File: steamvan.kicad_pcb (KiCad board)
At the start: 2 copper layers, 243.4 x 76.7 mm, 188 parts, among them J1 Conn_01x05_Male, Q1 FMMT493TA, SW1 SW_Push, U1 STM32F303CBTx, U2 TLV70233_SOT23-5, U3 NUF2221W1T2G, U4 74LVC1G34, Y1 8MHz

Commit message: Update: Move more components
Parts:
- moved R40 1.10 mm to (143.4, 127.0)
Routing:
- net Net-(K_SUPER1-Pad4): track 10.2 -> 8.71 mm
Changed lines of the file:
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@@
     (thickness 1.6)
     (drawings 6)
-    (tracks 2157)
+    (tracks 2158)
     (zones 0)
     (modules 188)
@@
   )
   (module Resistor_SMD:R_0603_1608Metric (layer B.Cu)
-    (at 144.4625 127 90)
+    (at 143.3576 127 90)
     (descr "Resistor SMD 0603 (1608 Metric), square (rectangular) end terminal, IPC_7351 nominal, (Body size source: http://www.tortai-tech.com/upload/download/2011102023233369053.pdf), generated with kicad-footprint-generator")
     (tags resistor)
@@
   (via (at 233.299 107.442) (size 0.8) (drill 0.4) (layers F.Cu B.Cu) (net 2))
   (via (at 218.313 127.381) (size 0.8) (drill 0.4) (layers F.Cu B.Cu) (net 2))
-  (via (at 142.367 128.27) (size 0.8) (drill 0.4) (layers F.Cu B.Cu) (net 2))
+  (via (at 141.3764 128.4224) (size 0.8) (drill 0.4) (layers F.Cu B.Cu) (net 2))
   (via (at 97.282 110.617) (size 0.8) (drill 0.4) (layers F.Cu B.Cu) (net 2))
   (via (at 203.0984 127) (size 0.8) (drill 0.4) (layers F.Cu B.Cu) (net 2))
@@
   (segment (start 211.29 127.7875) (end 210.82 127.3175) (width 0.381) (layer B.Cu) (net 83) (status 30))
   (segment (start 215.9 127.7875) (end 211.29 127.7875) (width 0.381) (layer B.Cu) (net 83) (status 30))
-  (segment (start 144.4625 127.7875) (end 144.4625 128.4605) (width 0.381) (layer B.Cu) (net 84) (status 10))
-  (segment (start 144.4625 128.4605) (end 143.637 129.286) (width 0.381) (layer B.Cu) (net 84))
-  (segment (start 136.8425 128.651) (end 136.8425 127.3175) (width 0.381) (layer B.Cu) (net 84) (status 20))
-  (segment (start 137.4775 129.286) (end 136.8425 128.651) (width 0.381) (layer B.Cu) (net 84))
-  (segment (start 143.637 129.286) (end 137.4775 129.286) (width 0.381) (layer B.Cu) (net 84))
+  (segment (start 143.3576 127.7875) (end 143.3576 128.27) (width 0.381) (layer B.Cu) (net 84))
+  (segment (start 143.3576 127.7875) (end 143.3576 128.1176) (width 0.381) (layer B.Cu) (net 84))
+  (segment (start 143.3576 128.1176) (end 142.0876 129.3876) (width 0.381) (layer B.Cu) (net 84))
+  (segment (start 138.9126 129.3876) (end 136.8425 127.3175) (width 0.381) (layer B.Cu) (net 84))
+  (segment (start 142.0876 129.3876) (end 138.9126 129.3876) (width 0.381) (layer B.Cu) (net 84))
   (segment (start 178.689 68.961) (end 177.4825 70.1675) (width 0.381) (layer B.Cu) (net 85) (status 20))
   (segment (start 184.15 70.6375) (end 182.4735 68.961) (width 0.381) (layer B.Cu) (net 85) (status 10))
@@
   (segment (start 160.3375 107.1625) (end 160.9345 107.1625) (width 0.381) (layer B.Cu) (net 93) (status 10))
   (segment (start 160.9345 107.1625) (end 161.798 106.299) (width 0.381) (layer B.Cu) (net 93))
-  (segment (start 174.58065 125.3744) (end 175.41875 126.2125) (width 0.381) (layer B.Cu) (net 93) (status 20))
-  (segment (start 144.4625 126.2125) (end 145.3006 125.3744) (width 0.381) (layer B.Cu) (net 93) (status 10))
-  (segment (start 145.3006 125.3744) (end 174.58065 125.3744) (width 0.381) (layer B.Cu) (net 93))
-  (segment (start 123.825 126.2125) (end 124.675789 125.361711) (width 0.381) (layer B.Cu) (net 93) (status 10))
-  (segment (start 143.611711 125.361711) (end 144.4625 126.2125) (width 0.381) (layer B.Cu) (net 93) (status 20))
-  (segment (start 124.675789 125.361711) (end 143.611711 125.361711) (width 0.381) (layer B.Cu) (net 93))
   (segment (start 283.7688 86.4362) (end 283.7688 78.0288) (width 0.381) (layer F.Cu) (net 93))
   (via (at 278.384 70.231) (size 0.8) (drill 0.4) (layers F.Cu B.Cu) (net 93))
@@
   (segment (start 274.828 124.7775) (end 273.361099 126.244401) (width 0.381) (layer F.Cu) (net 93))
   (segment (start 271.113785 107.3023) (end 275.113711 111.302226) (width 0.381) (layer F.Cu) (net 93))
+  (segment (start 144.1957 125.3744) (end 143.3576 126.2125) (width 0.381) (layer B.Cu) (net 93))
+  (segment (start 175.41875 126.2125) (end 174.58065 125.3744) (width 0.381) (layer B.Cu) (net 93))
+  (segment (start 174.58065 125.3744) (end 144.1957 125.3744) (width 0.381) (layer B.Cu) (net 93))
+  (segment (start 123.825 126.2125) (end 132.8167 126.2125) (width 0.381) (layer B.Cu) (net 93))
+  (segment (start 132.8167 126.2125) (end 133.4516 125.5776) (width 0.381) (layer B.Cu) (net 93))
+  (segment (start 142.7227 125.5776) (end 143.3576 126.2125) (width 0.381) (layer B.Cu) (net 93))
+  (segment (start 133.4516 125.5776) (end 142.7227 125.5776) (width 0.381) (layer B.Cu) (net 93))
   (segment (start 276.7836 77.3684) (end 275.844 78.308) (width 0.254) (layer B.Cu) (net 94) (status 20))
   (segment (start 282.8576 77.3684) (end 276.7836 77.3684) (width 0.254) (layer B.Cu) (net 94))

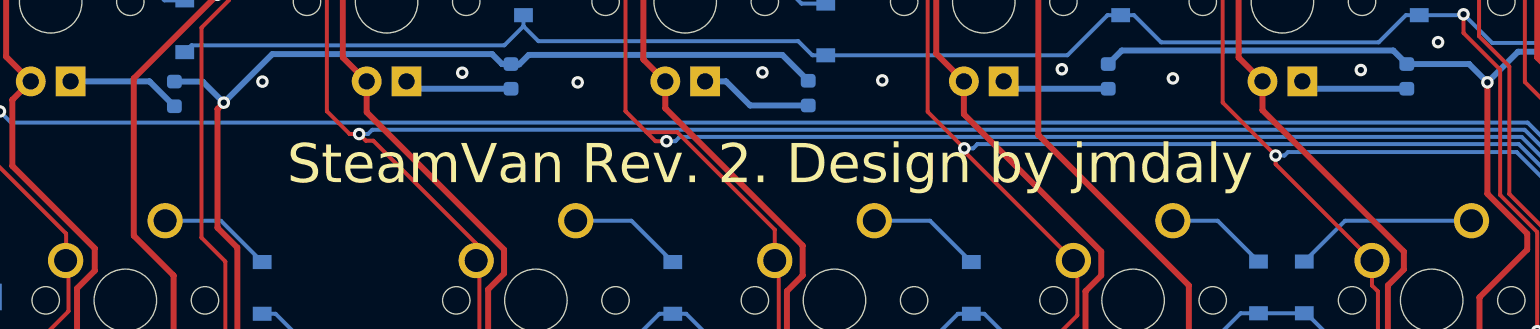
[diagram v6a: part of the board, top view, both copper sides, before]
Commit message: Update: Files for KiCad 5.1
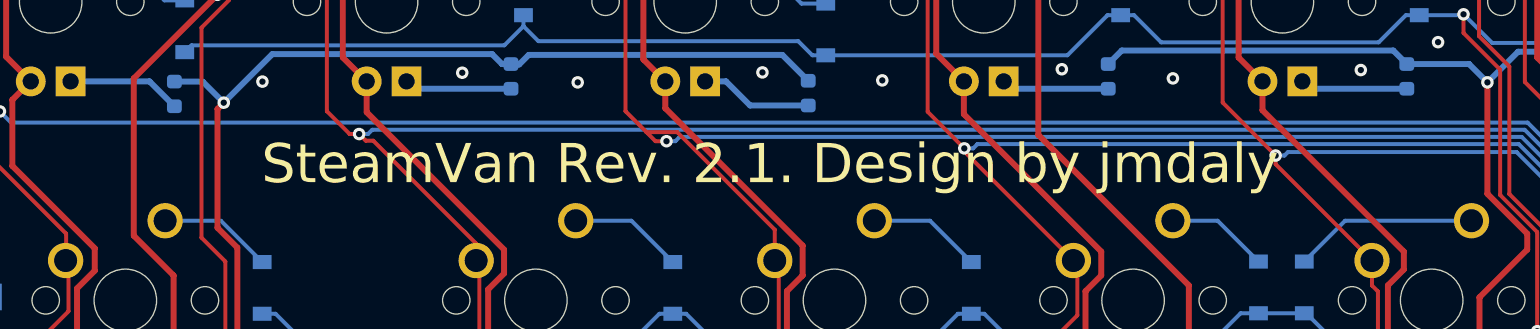
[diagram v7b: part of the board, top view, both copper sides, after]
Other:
- board text added: "SteamVan Rev. 2.1. Design by jmdaly"
- board text removed: "SteamVan Rev. 2. Design by jmdaly"
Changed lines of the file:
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@@
-(kicad_pcb (version 20171130) (host pcbnew 5.0.2-bee76a0~70~ubuntu16.04.1)
+(kicad_pcb (version 20171130) (host pcbnew 5.1.5-52549c5~84~ubuntu16.04.1)
   (general
     (thickness 1.6)
@@
     (zone_45_only no)
     (trace_min 0.2)
-    (segment_width 0.2)
-    (edge_width 0.15)
     (via_size 0.8)
     (via_drill 0.4)
@@
     (uvia_min_size 0.2)
     (uvia_min_drill 0.1)
+    (edge_width 0.15)
+    (segment_width 0.2)
     (pcb_text_width 0.3)
     (pcb_text_size 1.5 1.5)
@@
     (add_net "Net-(K_Z1-Pad4)")
   )
+  (module Type-C:HRO-TYPE-C-31-M-12-Assembly (layer B.Cu)
+    (at 284.584 53.646)
+    (attr smd)
+    (fp_text reference USB1 (at 0 9.25) (layer B.SilkS)
+      (effects (font (size 1 1) (thickness 0.15)) (justify mirror))
+    )
+    (fp_text value HRO-TYPE-C-31-M-12 (at 0 -1.15) (layer Dwgs.User)
+      (effects (font (size 1 1) (thickness 0.15)))
+    )
+    (fp_line (start 3.75 8.5) (end 3.75 7.5) (layer B.CrtYd) (width 0.15))
+    (fp_line (start -3.75 8.5) (end 3.75 8.5) (layer B.CrtYd) (width 0.15))
+    (fp_line (start -3.75 7.5) (end -3.75 8.5) (layer B.CrtYd) (width 0.15))
+    (fp_line (start -4.5 0) (end -4.5 7.5) (layer B.CrtYd) (width 0.15))
+    (fp_line (start 4.5 0) (end -4.5 0) (layer B.CrtYd) (width 0.15))
+    (fp_line (start 4.5 7.5) (end 4.5 0) (layer B.CrtYd) (width 0.15))
+    (fp_line (start 3.75 7.5) (end 4.5 7.5) (layer B.CrtYd) (width 0.15))
+    (fp_line (start -4.5 7.5) (end -3.75 7.5) (layer B.CrtYd) (width 0.15))
+    (fp_text user %R (at 0 9.25) (layer B.Fab)
+      (effects (font (size 1 1) (thickness 0.15)) (justify mirror))
+    )
+    (fp_line (start -4.47 0) (end 4.47 0) (layer Dwgs.User) (width 0.15))
+    (fp_line (start -4.47 0) (end -4.47 7.3) (layer Dwgs.User) (width 0.15))
+    (fp_line (start 4.47 0) (end 4.47 7.3) (layer Dwgs.User) (width 0.15))
+    (fp_line (start -4.47 7.3) (end 4.47 7.3) (layer Dwgs.User) (width 0.15))
+    (pad 12 smd rect (at 3.225 7.695) (size 0.6 1.45) (layers B.Cu B.Paste B.Mask)
+      (net 2 GND))
+    (pad 1 smd rect (at -3.225 7.695) (size 0.6 1.45) (layers B.Cu B.Paste B.Mask)
+      (net 2 GND))
+    (pad 11 smd rect (at 2.45 7.695) (size 0.6 1.45) (layers B.Cu B.Paste B.Mask)
+      (net 34 "Net-(F1-Pad2)"))
+    (pad 2 smd rect (at -2.45 7.695) (size 0.6 1.45) (layers B.Cu B.Paste B.Mask)
+      (net 34 "Net-(F1-Pad2)"))
+    (pad 3 smd rect (at -1.75 7.695) (size 0.3 1.45) (layers B.Cu B.Paste B.Mask)
+      (net 112 "Net-(USB1-Pad3)"))
+    (pad 10 smd rect (at 1.75 7.695) (size 0.3 1.45) (layers B.Cu B.Paste B.Mask)
+      (net 97 "Net-(RC7-Pad2)"))
+    (pad 4 smd rect (at -1.25 7.695) (size 0.3 1.45) (layers B.Cu B.Paste B.Mask)
+      (net 96 "Net-(RC6-Pad2)"))
+    (pad 9 smd rect (at 1.25 7.695) (size 0.3 1.45) (layers B.Cu B.Paste B.Mask)
+      (net 111 "Net-(USB1-Pad9)"))
+    (pad 5 smd rect (at -0.75 7.695) (size 0.3 1.45) (layers B.Cu B.Paste B.Mask)
+      (net 110 D_NI))
+    (pad 8 smd rect (at 0.75 7.695) (size 0.3 1.45) (layers B.Cu B.Paste B.Mask)
+      (net 109 D_PI))
+    (pad 7 smd rect (at 0.25 7.695) (size 0.3 1.45) (layers B.Cu B.Paste B.Mask)
+      (net 110 D_NI))
+    (pad 6 smd rect (at -0.25 7.695) (size 0.3 1.45) (layers B.Cu B.Paste B.Mask)
+      (net 109 D_PI))
+    (pad "" np_thru_hole circle (at 2.89 6.25) (size 0.65 0.65) (drill 0.65) (layers *.Cu *.Mask))
+    (pad "" np_thru_hole circle (at -2.89 6.25) (size 0.65 0.65) (drill 0.65) (layers *.Cu *.Mask))
+    (pad 13 thru_hole oval (at -4.32 6.78) (size 1 2.1) (drill oval 0.6 1.7) (layers *.Cu *.Mask)
+      (net 2 GND))
+    (pad 13 thru_hole oval (at 4.32 6.78) (size 1 2.1) (drill oval 0.6 1.7) (layers *.Cu *.Mask)
+      (net 2 GND))
+    (pad 13 thru_hole oval (at -4.32 2.6) (size 1 1.6) (drill oval 0.6 1.2) (layers *.Cu *.Mask)
+      (net 2 GND))
+    (pad 13 thru_hole oval (at 4.32 2.6) (size 1 1.6) (drill oval 0.6 1.2) (layers *.Cu *.Mask)
+      (net 2 GND))
+  )
   (module jmdaly_keyboard_parts:minivan_outline locked (layer F.Cu)
     (at 102.84 74.63)
@@
       (net 105 D_N))
   )
-  (module Type-C:HRO-TYPE-C-31-M-12-Assembly (layer B.Cu)
-    (at 284.584 53.646)
-    (fp_text reference USB1 (at 0 9.25) (layer B.SilkS)
-      (effects (font (size 1 1) (thickness 0.15)) (justify mirror))
-    )
-    (fp_text value HRO-TYPE-C-31-M-12 (at 0 -1.15) (layer Dwgs.User)
-      (effects (font (size 1 1) (thickness 0.15)))
-    )
-    (fp_line (start -4.47 7.3) (end 4.47 7.3) (layer Dwgs.User) (width 0.15))
-    (fp_line (start 4.47 0) (end 4.47 7.3) (layer Dwgs.User) (width 0.15))
-    (fp_line (start -4.47 0) (end -4.47 7.3) (layer Dwgs.User) (width 0.15))
-    (fp_line (start -4.47 0) (end 4.47 0) (layer Dwgs.User) (width 0.15))
-    (fp_text user %R (at 0 9.25) (layer B.Fab)
-      (effects (font (size 1 1) (thickness 0.15)) (justify mirror))
-    )
-    (fp_line (start -4.5 7.5) (end 4.5 7.5) (layer B.CrtYd) (width 0.15))
-    (fp_line (start 4.5 7.5) (end 4.5 0) (layer B.CrtYd) (width 0.15))
-    (fp_line (start 4.5 0) (end -4.5 0) (layer B.CrtYd) (width 0.15))
-    (fp_line (start -4.5 0) (end -4.5 7.5) (layer B.CrtYd) (width 0.15))
-    (fp_line (start -3.75 7.5) (end -3.75 8.5) (layer B.CrtYd) (width 0.15))
-    (fp_line (start -3.75 8.5) (end 3.75 8.5) (layer B.CrtYd) (width 0.15))
-    (fp_line (start 3.75 8.5) (end 3.75 7.5) (layer B.CrtYd) (width 0.15))
-    (pad 13 thru_hole oval (at 4.32 2.6) (size 1 1.6) (drill oval 0.6 1.2) (layers *.Cu *.Mask)
-      (net 2 GND))
-    (pad 13 thru_hole oval (at -4.32 2.6) (size 1 1.6) (drill oval 0.6 1.2) (layers *.Cu *.Mask)
-      (net 2 GND))
-    (pad 13 thru_hole oval (at 4.32 6.78) (size 1 2.1) (drill oval 0.6 1.7) (layers *.Cu *.Mask)
-      (net 2 GND))
-    (pad 13 thru_hole oval (at -4.32 6.78) (size 1 2.1) (drill oval 0.6 1.7) (layers *.Cu *.Mask)
-      (net 2 GND))
-    (pad "" np_thru_hole circle (at -2.89 6.25) (size 0.65 0.65) (drill 0.65) (layers *.Cu *.Mask))
-    (pad "" np_thru_hole circle (at 2.89 6.25) (size 0.65 0.65) (drill 0.65) (layers *.Cu *.Mask))
-    (pad 6 smd rect (at -0.25 7.695) (size 0.3 1.45) (layers B.Cu B.Paste B.Mask)
-      (net 109 D_PI))
-    (pad 7 smd rect (at 0.25 7.695) (size 0.3 1.45) (layers B.Cu B.Paste B.Mask)
-      (net 110 D_NI))
-    (pad 8 smd rect (at 0.75 7.695) (size 0.3 1.45) (layers B.Cu B.Paste B.Mask)
-      (net 109 D_PI))
-    (pad 5 smd rect (at -0.75 7.695) (size 0.3 1.45) (layers B.Cu B.Paste B.Mask)
-      (net 110 D_NI))
-    (pad 9 smd rect (at 1.25 7.695) (size 0.3 1.45) (layers B.Cu B.Paste B.Mask)
-      (net 111 "Net-(USB1-Pad9)"))
-    (pad 4 smd rect (at -1.25 7.695) (size 0.3 1.45) (layers B.Cu B.Paste B.Mask)
-      (net 96 "Net-(RC6-Pad2)"))
-    (pad 10 smd rect (at 1.75 7.695) (size 0.3 1.45) (layers B.Cu B.Paste B.Mask)
-      (net 97 "Net-(RC7-Pad2)"))
-    (pad 3 smd rect (at -1.75 7.695) (size 0.3 1.45) (layers B.Cu B.Paste B.Mask)
-      (net 112 "Net-(USB1-Pad3)"))
-    (pad 2 smd rect (at -2.45 7.695) (size 0.6 1.45) (layers B.Cu B.Paste B.Mask)
-      (net 34 "Net-(F1-Pad2)"))
-    (pad 11 smd rect (at 2.45 7.695) (size 0.6 1.45) (layers B.Cu B.Paste B.Mask)
-      (net 34 "Net-(F1-Pad2)"))
-    (pad 1 smd rect (at -3.225 7.695) (size 0.6 1.45) (layers B.Cu B.Paste B.Mask)
-      (net 2 GND))
-    (pad 12 smd rect (at 3.225 7.695) (size 0.6 1.45) (layers B.Cu B.Paste B.Mask)
-      (net 2 GND))
-  )
   (module Crystal:Crystal_SMD_5032-4Pin_5.0x3.2mm (layer B.Cu)
     (at 189.738 127.381)
@@
     (effects (font (size 1 1) (thickness 0.125)) (justify mirror))
   )
-  (gr_text "SteamVan Rev. 2. Design by jmdaly" (at 129.2352 94.488) (layer F.SilkS)
+  (gr_text "SteamVan Rev. 2.1. Design by jmdaly" (at 129.2352 94.488) (layer F.SilkS)
     (effects (font (size 2.5 2.5) (thickness 0.3)))
   )
